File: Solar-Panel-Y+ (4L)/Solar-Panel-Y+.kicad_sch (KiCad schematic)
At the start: 73 parts, among them J1 FTS-105-01-L-DV-A, Q1 BSS138DWQ-7, Q2 MBT2222ADW1T1, Q3 BSS138DWQ-7, Q4 MBT2222ADW1T1, U1 Value, U2 TSL2561

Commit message: Changed TSL2591 to BH1750
All boards (4L) except -Y
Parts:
- removed U2: TSL2561, solarpanels:TSL2561, symbol solarpanels:symbols_TSL2561
- added U2: BH1750FVI-TR, WSOF6, symbol solarpanels:BH1750FVI-TR
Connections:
- net +3V3: now also U2.1 (VCC)
- net GND: now also U2.3 (GND)
- net SCL_LS: now also U2.6 (SCL)
- net SDA_LS: now also U2.4 (SDA)
- net at R1.2, R2.1: now also U2.2 (ADDR)
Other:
- moved on the sheet: C11, C3, C6, D1, D2, D5, H1, H2, H3, H4, J1, R10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

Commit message: Updated light sensor to OPT 3001, Updated solar diodes.
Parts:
- removed C12, C13: 10nF, Capacitor_SMD:C_0603_1608Metric, symbol Device:C
- removed D5: MSS1P4-M3_89A, solarpanels:MICROSMP, symbol Device:D_Schottky
- removed Q1, Q3: BSS138DWQ-7, Package_TO_SOT_SMD:SOT-363_SC-70-6, symbol mainboard:BSS138DWQ-7
- removed Q2, Q4: MBT2222ADW1T1, Package_TO_SOT_SMD:SOT-363_SC-70-6, symbol Transistor_BJT:MBT2222ADW1T1
- removed R19, R20: DNI, Resistor_SMD:R_0603_1608Metric, symbol Device:R_US
- removed R21, R26: 680, Resistor_SMD:R_0603_1608Metric, symbol Device:R_US
- removed R22, R27: 100K, Resistor_SMD:R_0603_1608Metric, symbol Device:R_US
- removed R23, R24, R28, R29: 10K, Resistor_SMD:R_0603_1608Metric, symbol Device:R_US
- removed R25, R30: 200K, Resistor_SMD:R_0603_1608Metric, symbol Device:R_US
- removed U2: BH1750FVI-TR, WSOF6, symbol solarpanels:BH1750FVI-TR
- added U2: OPT3001, solarpanels:OPT3001, symbol solarpanels:OPT3001
- added U3: MAX40200AUK, Package_TO_SOT_SMD:SOT-23-5, symbol Analog_Switch:MAX40200AUK
- D2, D3, D4: value MSS1P4-M3_89A -> DFLS130L-7; footprint solarpanels:MICROSMP -> Diode_SMD:D_PowerDI-123; Allied Price/Stock https://www.alliedelec.com/general-semiconductor-vishay-mss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 -> (none); Allied_Number 70217632 -> (none); Manufacturer_Name Vishay -> (none); Manufacturer_Part_Number MSS1P4-M3/89A -> (none); Mouser Part Number 625-MSS1P4-M3 -> (none); Mouser Price/Stock https://www.mouser.com/Search/Refine.aspx?Keyword=625-MSS1P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 -> (none); RS Part Number 7103068P -> (none); RS Price/Stock http://uk.rs-online.com/web/p/products/7103068P -> (none)
- J1: value FTS-105-01-L-DV-A -> FTS-105-01-X-DV-A
- R1, R12, R13, R16, R17, R18, R2, R3, R4: value 0 -> 0R; symbol Device:R_US -> Device:R_Small_US
- R10, R11, R5, R6, R7, R8, R9: symbol Device:R_US -> Device:R_Small_US
- R14, R15: value DNI -> DNI (0R); symbol Device:R_US -> Device:R_Small_US
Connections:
- net +3V3: now also U2.1 (VDD), U3.5 (OUT); no longer D2.1 (K)
- net GND: now also U2.3 (GND), U2.7 (GND), U3.2 (GND)
- net SCL_LS: now also U2.4 (SCL)
- net SDA_LS: now also U2.6 (SDA)
- net VSOLAR: now also D2.1 (K)
- net VSOLAR_FULL: now also D2.2 (A)
- net at R1.2, R2.1: now also U2.2 (ADDR)
- net at C10.1, C8.1, L2.2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: now also U3.1 (VDD), U3.3 (EN); no longer D2.2 (A)
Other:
- added sheet Bus Protection (BusProtection.kicad_sch)
- note removed: "I2C Bus Protection - Light Sensor"
- moved on the sheet: C1, C11

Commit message: B3/02 Updates
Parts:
- C1: value 1uF -> 0.1uF
- H1, H2, H3, H4: footprint MountingHole:MountingHole_2.2mm_M2_DIN965_Pad -> solarpanels:MountingHole_2.2mm_M2_DIN965_Pad_TopBottom; now left out of the parts list
- TP1, TP2, TP3, TP4: now left out of the parts list
- U1: value Value -> BQ25570RGRR
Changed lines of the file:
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@@
   (title_block
     (title "PyCubed Mini")
-    (date "2023-02-19")
-    (rev "Rev B3/01")
+    (date "2023-04-12")
+    (rev "Rev B3/02")
     (company "REx Lab Carnegie Mellon University")
     (comment 1 "Z.Manchester")
@@
       (effects (font (size 1.27 1.27)) (justify left))
     )
-    (property "Value" "1uF" (at 15.113 178.181 0)
+    (property "Value" "0.1uF" (at 13.335 178.054 0)
       (effects (font (size 1.27 1.27)) (justify left))
     )
@@
   )
   (symbol (lib_id "Connector:TestPoint") (at 199.39 173.99 0) (unit 1)
-    (in_bom yes) (on_board yes) (dnp no)
+    (in_bom no) (on_board yes) (dnp no)
     (property "Reference" "TP2" (at 197.612 168.783 0)
       (effects (font (size 1.27 1.27)) (justify left))
@@
   )
   (symbol (lib_id "Connector:TestPoint") (at 205.74 173.99 0) (unit 1)
-    (in_bom yes) (on_board yes) (dnp no)
+    (in_bom no) (on_board yes) (dnp no)
     (property "Reference" "TP3" (at 203.962 168.783 0)
       (effects (font (size 1.27 1.27)) (justify left))
@@
   )
   (symbol (lib_id "Connector:TestPoint") (at 212.09 173.99 0) (unit 1)
-    (in_bom yes) (on_board yes) (dnp no)
+    (in_bom no) (on_board yes) (dnp no)
     (property "Reference" "TP4" (at 210.312 168.783 0)
       (effects (font (size 1.27 1.27)) (justify left))
@@
   )
   (symbol (lib_id "Connector:TestPoint") (at 193.04 173.99 0) (unit 1)
-    (in_bom yes) (on_board yes) (dnp no)
+    (in_bom no) (on_board yes) (dnp no)
     (property "Reference" "TP1" (at 191.262 168.783 0)
       (effects (font (size 1.27 1.27)) (justify left))
@@
       (effects (font (size 1.7526 1.7526)) (justify left bottom))
     )
-    (property "Value" "Value" (at 111.4806 74.7014 0)
+    (property "Value" "BQ25570RGRR" (at 111.4806 74.7014 0)
       (effects (font (size 1.7526 1.7526)) (justify left bottom) hide)
     )
@@
   )
   (symbol (lib_id "Mechanical:MountingHole_Pad") (at 196.85 128.27 270) (unit 1)
-    (in_bom yes) (on_board yes) (dnp no)
+    (in_bom no) (on_board yes) (dnp no)
     (property "Reference" "H4" (at 201.422 127.381 90)
       (effects (font (size 1.27 1.27)) (justify left))
@@
       (effects (font (size 1.27 1.27)) (justify left))
     )
-    (property "Footprint" "MountingHole:MountingHole_2.2mm_M2_DIN965_Pad" (at 196.85 128.27 0)
+    (property "Footprint" "solarpanels:MountingHole_2.2mm_M2_DIN965_Pad_TopBottom" (at 196.85 128.27 0)
       (effects (font (size 1.27 1.27)) hide)
     )
@@
   )
   (symbol (lib_id "Mechanical:MountingHole_Pad") (at 196.85 109.22 270) (unit 1)
-    (in_bom yes) (on_board yes) (dnp no)
+    (in_bom no) (on_board yes) (dnp no)
     (property "Reference" "H1" (at 201.422 108.204 90)
       (effects (font (size 1.27 1.27)) (justify left))
@@
       (effects (font (size 1.27 1.27)) (justify left))
     )
-    (property "Footprint" "MountingHole:MountingHole_2.2mm_M2_DIN965_Pad" (at 196.85 109.22 0)
+    (property "Footprint" "solarpanels:MountingHole_2.2mm_M2_DIN965_Pad_TopBottom" (at 196.85 109.22 0)
       (effects (font (size 1.27 1.27)) hide)
     )
@@
   )
   (symbol (lib_id "Mechanical:MountingHole_Pad") (at 196.85 115.57 270) (unit 1)
-    (in_bom yes) (on_board yes) (dnp no)
+    (in_bom no) (on_board yes) (dnp no)
     (property "Reference" "H2" (at 201.422 114.554 90)
       (effects (font (size 1.27 1.27)) (justify left))
@@
       (effects (font (size 1.27 1.27)) (justify left))
     )
-    (property "Footprint" "MountingHole:MountingHole_2.2mm_M2_DIN965_Pad" (at 196.85 115.57 0)
+    (property "Footprint" "solarpanels:MountingHole_2.2mm_M2_DIN965_Pad_TopBottom" (at 196.85 115.57 0)
       (effects (font (size 1.27 1.27)) hide)
     )
@@
   )
   (symbol (lib_id "Mechanical:MountingHole_Pad") (at 196.85 121.92 270) (unit 1)
-    (in_bom yes) (on_board yes) (dnp no)
+    (in_bom no) (on_board yes) (dnp no)
     (property "Reference" "H3" (at 201.422 120.904 90)
       (effects (font (size 1.27 1.27)) (justify left))
@@
       (effects (font (size 1.27 1.27)) (justify left))
     )
-    (property "Footprint" "MountingHole:MountingHole_2.2mm_M2_DIN965_Pad" (at 196.85 121.92 0)
-      (effects (font (size 1.27 1.27)) hide)
-    )
+    (property "Footprint" "solarpanels:MountingHole_2.2mm_M2_DIN965_Pad_TopBottom" (at 196.85 121.92 0)
+      (effects (font (size 1.27 1.27)) hide)
+    )

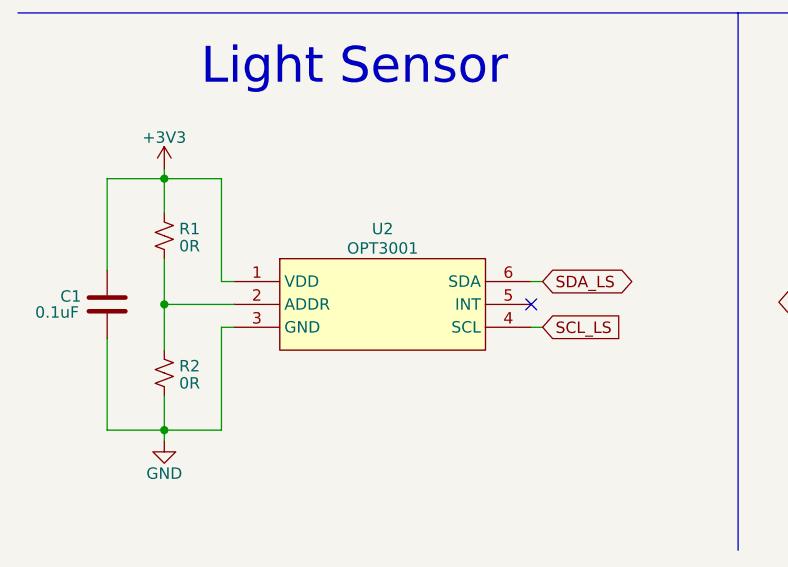
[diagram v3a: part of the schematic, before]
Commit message: Updated Sun Sensor to OPT4001
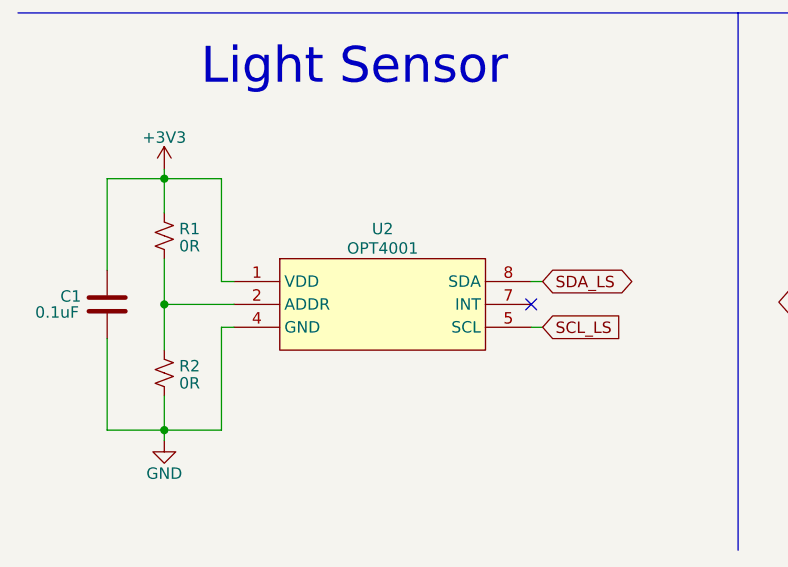
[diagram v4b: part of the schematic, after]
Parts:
- U2: value OPT3001 -> OPT4001; footprint solarpanels:OPT3001 -> Package_TO_SOT_SMD:SOT-583-8; symbol solarpanels:OPT3001 -> solarpanels:OPT4001
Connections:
- net GND: now also U2.4 (GND); no longer U2.3 (GND), U2.7 (GND)
- net SCL_LS: now also U2.5 (SCL); no longer U2.4 (SCL)
- net SDA_LS: now also U2.8 (SDA); no longer U2.6 (SDA)
- new net: U2.3 (NC), U2.6 (NC)
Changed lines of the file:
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@@
     )
   )
-  (symbol (lib_id "solarpanels:OPT3001") (at 51.943 177.165 0) (unit 1)
+  (symbol (lib_id "solarpanels:OPT4001") (at 51.943 177.165 0) (unit 1)
     (in_bom yes) (on_board yes) (dnp no)
     (property "Reference" "U2" (at 51.943 168.783 0)
       (effects (font (size 1.27 1.27)))
     )
-    (property "Value" "OPT3001" (at 51.943 170.942 0)
+    (property "Value" "OPT4001" (at 51.943 170.942 0)
       (effects (font (size 1.27 1.27)))
     )
-    (property "Footprint" "solarpanels:OPT3001" (at 51.943 183.515 0)
+    (property "Footprint" "Package_TO_SOT_SMD:SOT-583-8" (at 51.943 183.515 0)
       (effects (font (size 1.27 1.27)) hide)
     )
@@
     (pin "6")
     (pin "7")
+    (pin "8")
     (instances
       (project "Solar-Panel-Y+"
